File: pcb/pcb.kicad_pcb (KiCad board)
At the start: 2 copper layers, 156.4 x 122.7 mm, 68 parts, among them SW1 SW_Push, SW10 SW_Push, SW11 SW_Push, SW12 SW_Push, SW13 SW_Push, SW14 SW_Push, SW15 SW_Push, SW16 SW_Push, SW17 SW_Push, SW18 SW_Push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

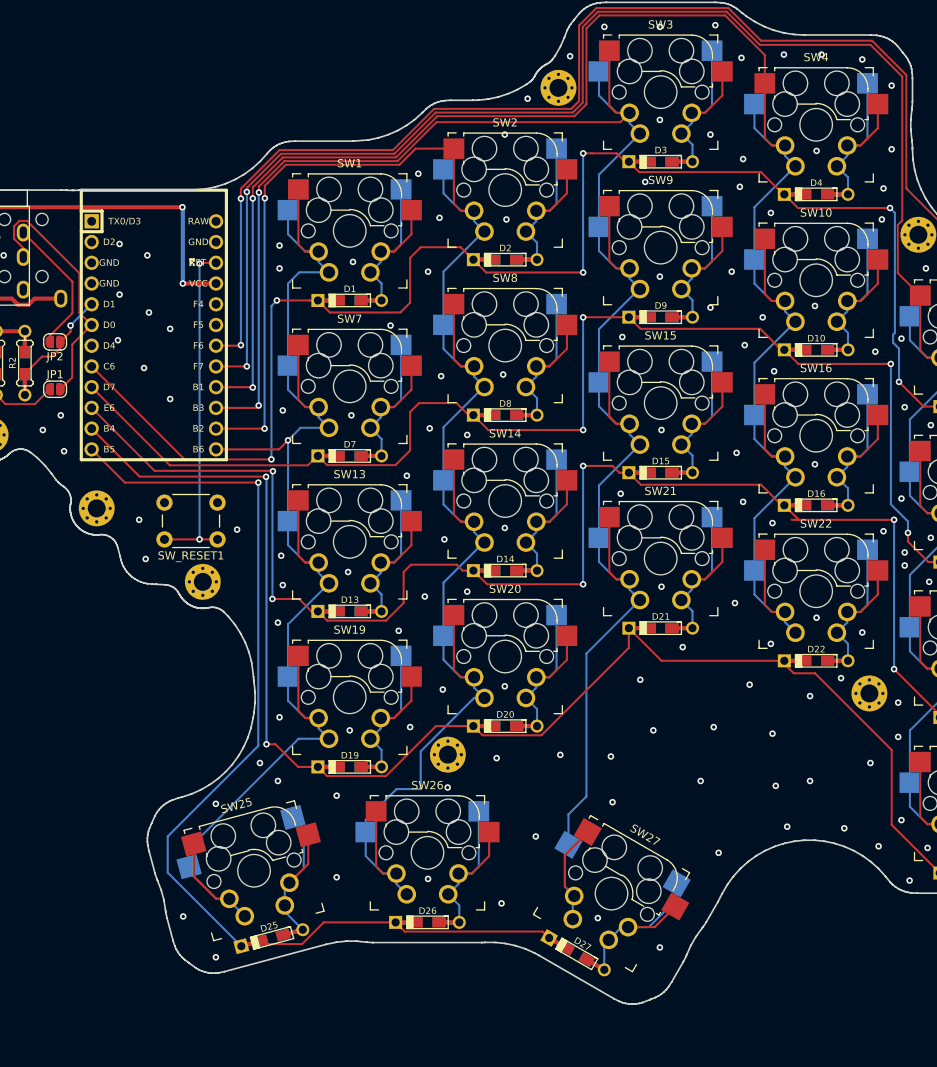
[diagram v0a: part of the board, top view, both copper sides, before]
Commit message: Redesign thumb cluster
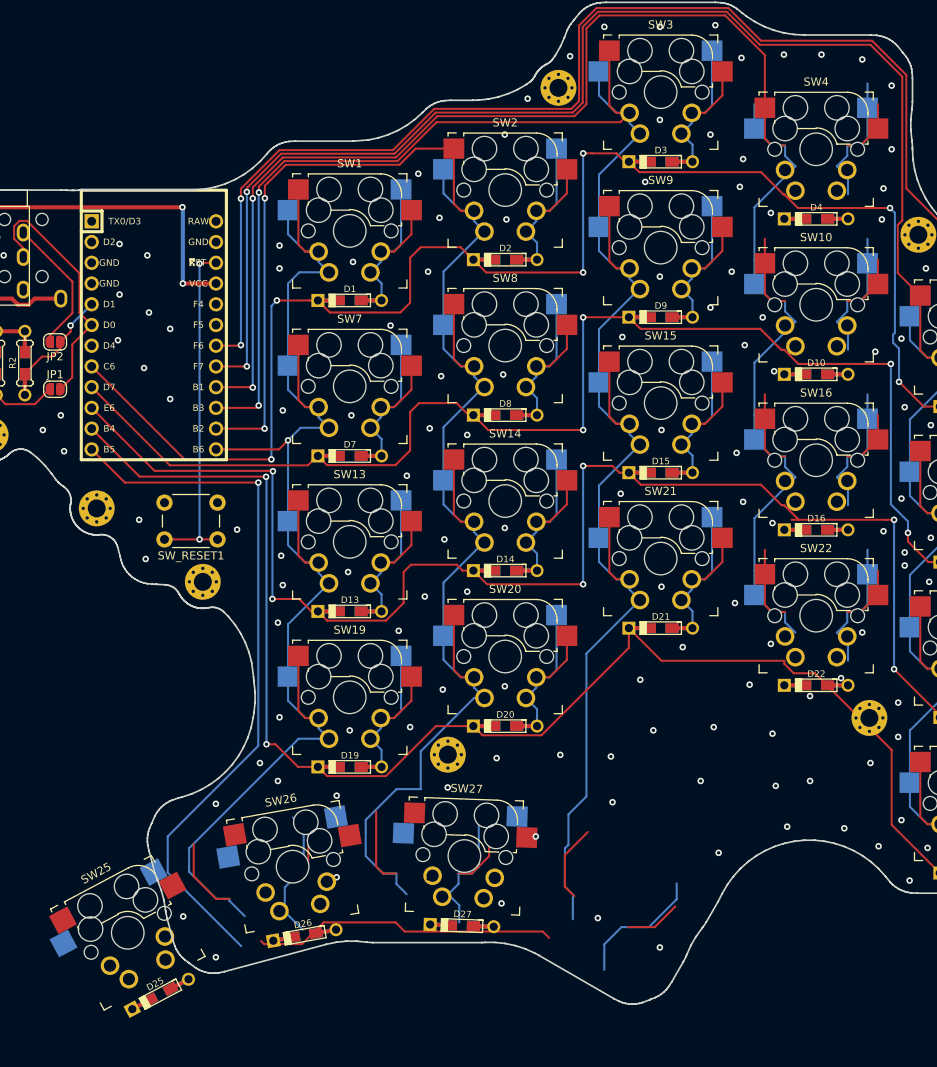
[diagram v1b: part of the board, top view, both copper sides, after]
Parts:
- moved SW27 18.6 mm to (14.1, 81.6), turned to 358 degrees
- moved SW25 17.2 mm to (-27.2, 91.0), turned to 28 degrees
- moved SW26 16.6 mm to (-7.00, 82.9), turned to 10 degrees
- moved D25 15.3 mm to (-23.2, 98.5), turned to 208 degrees
- moved D26 15.1 mm to (-5.52, 91.3), turned to 190 degrees
- moved D27 14.5 mm to (13.8, 90.1), turned to 178 degrees
- moved D4 3.00 mm to (57.1, 3.52)
- moved D10 3.00 mm to (57.1, 22.6)
- moved D16 3.00 mm to (57.1, 41.6)
- moved D22 3.00 mm to (57.1, 60.7)
- moved SW10 3.00 mm to (57.1, 14.1)
- moved SW16 3.00 mm to (57.1, 33.1)
- moved SW22 3.00 mm to (57.1, 52.1)
- moved SW4 3.00 mm to (57.1, -5.00)
- moved generated 3.00 mm to (63.7, 64.7)
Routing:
- net (no net): track 0.00 -> 43.0 mm, vias 0 -> 5
- net /row4: track 124.6 -> 87.2 mm
- net Net-(D25-Pad2): track 23.0 -> 0.00 mm, vias 0 -> 3
- net Net-(D26-Pad2): track 24.2 -> 37.4 mm, vias 0 -> 2
- net /col0: track 179.2 -> 169.7 mm
- net /col2: track 255.8 -> 263.0 mm, vias 2 -> 3
- net /col1: track 227.6 -> 234.2 mm
- net Net-(D27-Pad2): vias 0 -> 2
- net GND: vias 170 -> 157

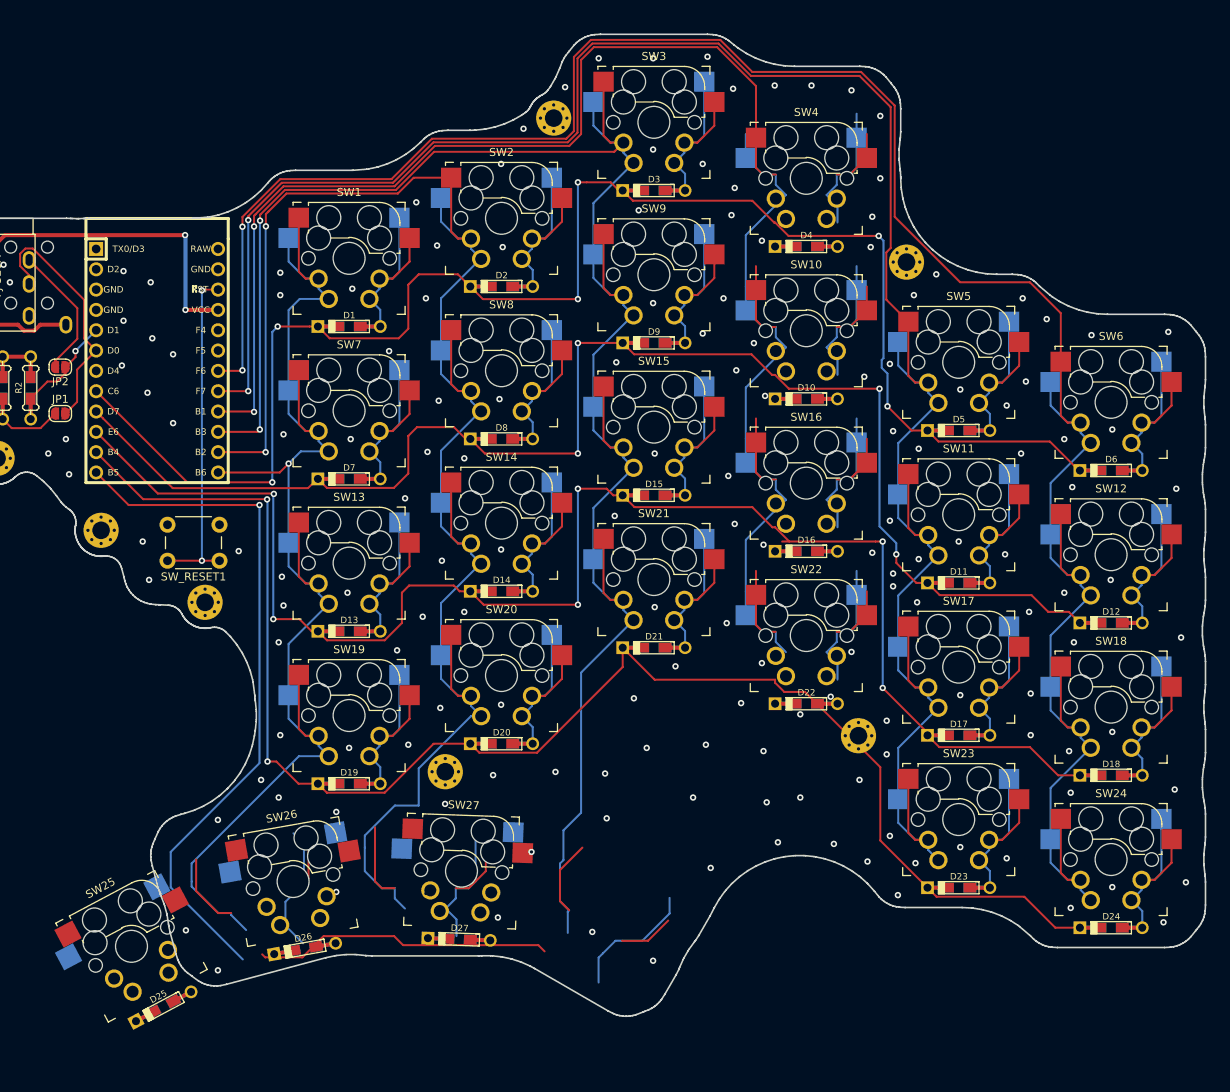
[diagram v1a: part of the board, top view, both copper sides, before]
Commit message: Adjust key placement
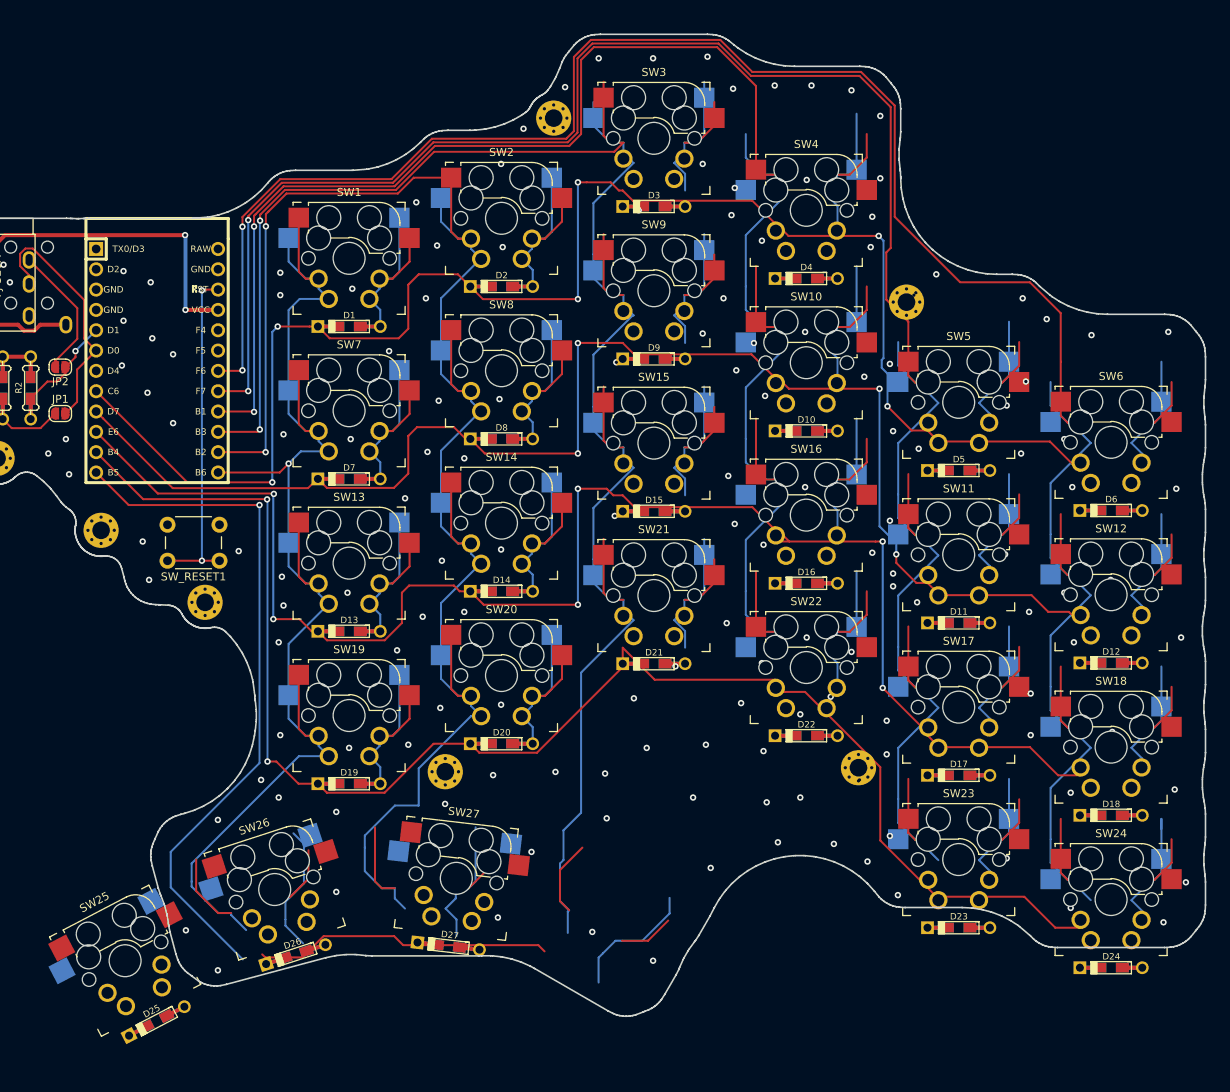
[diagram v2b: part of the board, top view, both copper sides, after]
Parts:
- removed the generated at (63.7, 64.7)
- removed the generated at (69.7, 5.47)
- added generated: MountingHole_2.2mm_M2_Pad_Via, MountingHole_2.2mm_M2_Pad_Via, F.Cu at (63.7, 68.7)
- added generated: MountingHole_2.2mm_M2_Pad_Via, MountingHole_2.2mm_M2_Pad_Via, F.Cu at (69.7, 10.5)
- moved D11 5.00 mm to (76.2, 50.6)
- moved D12 5.00 mm to (95.2, 55.6)
- moved D17 5.00 mm to (76.2, 69.6)
- moved D18 5.00 mm to (95.2, 74.6)
- moved D23 5.00 mm to (76.2, 88.7)
- moved D24 5.00 mm to (95.2, 93.7)
- moved D5 5.00 mm to (76.2, 31.5)
- moved D6 5.00 mm to (95.2, 36.5)
- moved SW11 5.00 mm to (76.2, 42.0)
- moved SW12 5.00 mm to (95.2, 47.0)
- moved SW17 5.00 mm to (76.2, 61.1)
- moved SW23 5.00 mm to (76.2, 80.2)
- moved SW24 5.00 mm to (95.2, 85.2)
- moved SW5 5.00 mm to (76.2, 23.0)
- moved SW6 5.00 mm to (95.2, 28.0)
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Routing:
- net (no net): track 43.0 -> 133.9 mm, vias 5 -> 25
- net /row4: track 87.2 -> 124.6 mm
- net Net-(D26-Pad2): track 37.4 -> 16.2 mm
- net Net-(D27-Pad2): track 23.1 -> 39.7 mm, vias 2 -> 1
- net /col2: track 263.0 -> 246.3 mm
- net /col1: track 234.2 -> 218.0 mm
- net Net-(D12-Pad2): track 24.2 -> 16.7 mm
- net Net-(D11-Pad2): track 24.2 -> 16.7 mm
- net Net-(D6-Pad2): track 24.2 -> 16.7 mm
- net Net-(D5-Pad2): track 24.2 -> 16.7 mm, vias 0 -> 1
- net Net-(D24-Pad2): track 25.5 -> 17.9 mm
- net Net-(D23-Pad2): track 24.2 -> 16.7 mm
- net Net-(D18-Pad2): track 24.2 -> 16.7 mm
- net Net-(D17-Pad2): track 24.2 -> 16.7 mm
- net Net-(D4-Pad2): track 24.2 -> 16.7 mm
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
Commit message: Update pcb
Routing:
- net (no net): track 133.9 -> 0.00 mm, vias 25 -> 1
- net /col0: track 169.7 -> 198.3 mm
- net /col1: track 218.0 -> 244.7 mm, vias 2 -> 3
- net Net-(D25-Pad2): track 0.00 -> 22.9 mm, vias 3 -> 0
- net Net-(D27-Pad2): track 39.7 -> 24.0 mm, vias 1 -> 0
- net /col2: track 246.3 -> 260.7 mm
- net Net-(D18-Pad2): track 16.7 -> 24.2 mm
- net Net-(D12-Pad2): track 16.7 -> 24.2 mm
- net Net-(D11-Pad2): track 16.7 -> 24.2 mm
- net Net-(D6-Pad2): track 16.7 -> 24.2 mm
- net Net-(D23-Pad2): track 16.7 -> 24.2 mm
- net Net-(D5-Pad2): track 16.7 -> 24.2 mm, vias 1 -> 0
- net Net-(D22-Pad2): track 16.7 -> 24.2 mm
- net Net-(D17-Pad2): track 16.7 -> 24.2 mm
- net Net-(D16-Pad2): track 16.7 -> 24.2 mm
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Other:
- board size 156.4 x 122.7 mm -> 156.4 x 127.2 mm

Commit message: Small tweaks, regenerate PCB
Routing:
- net GND: vias 101 -> 110

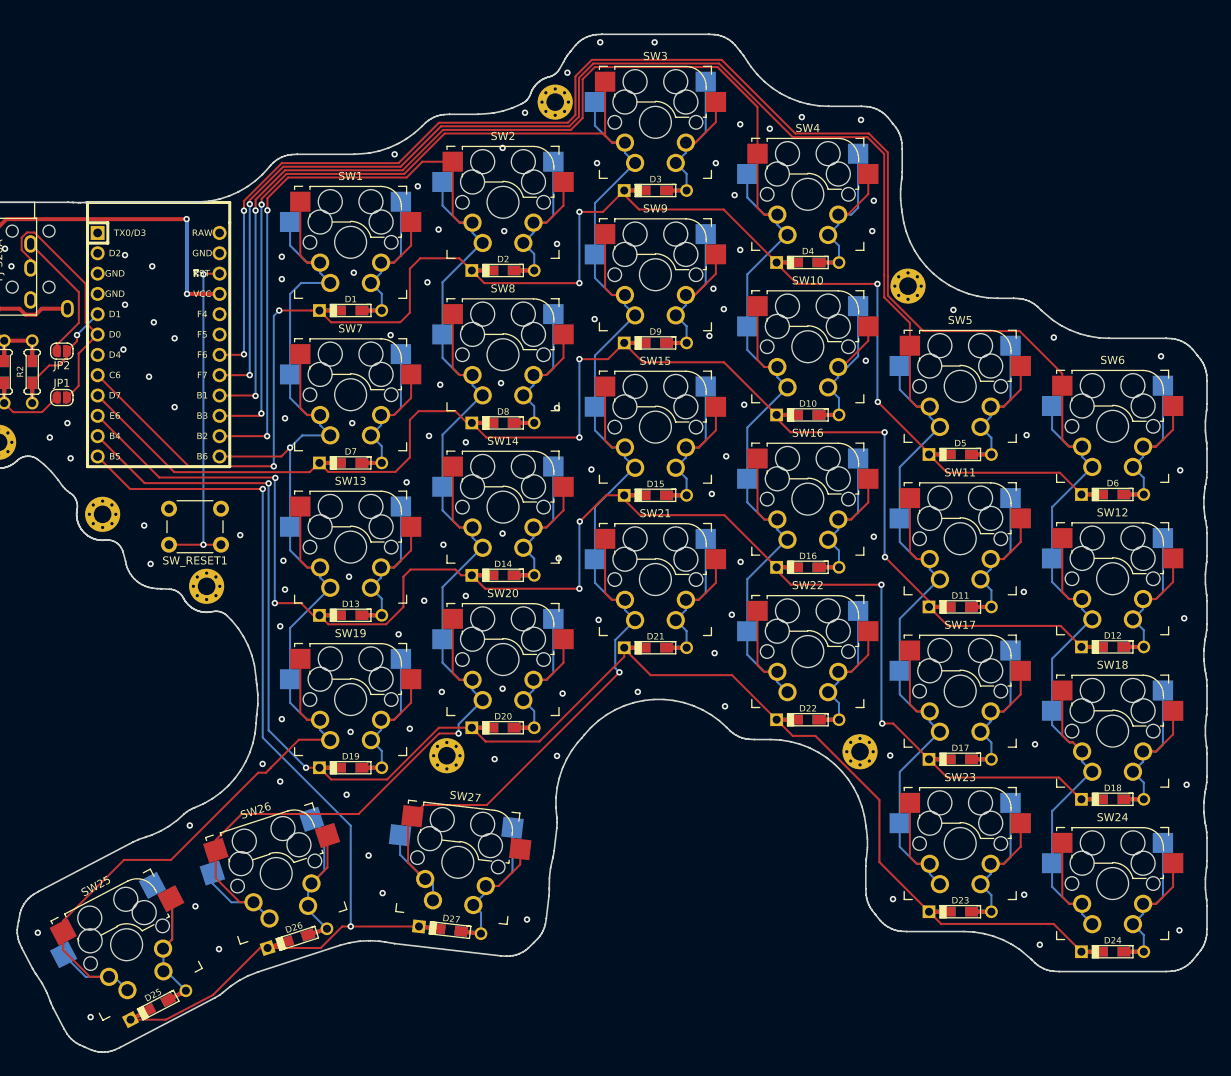
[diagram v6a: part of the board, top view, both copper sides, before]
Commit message: Change the column offsets post 1 fab
After 1 fab keyboard seemed to be too aggressive. Boo hoo.
Lessons learned. New measurments. And halfing it either way.
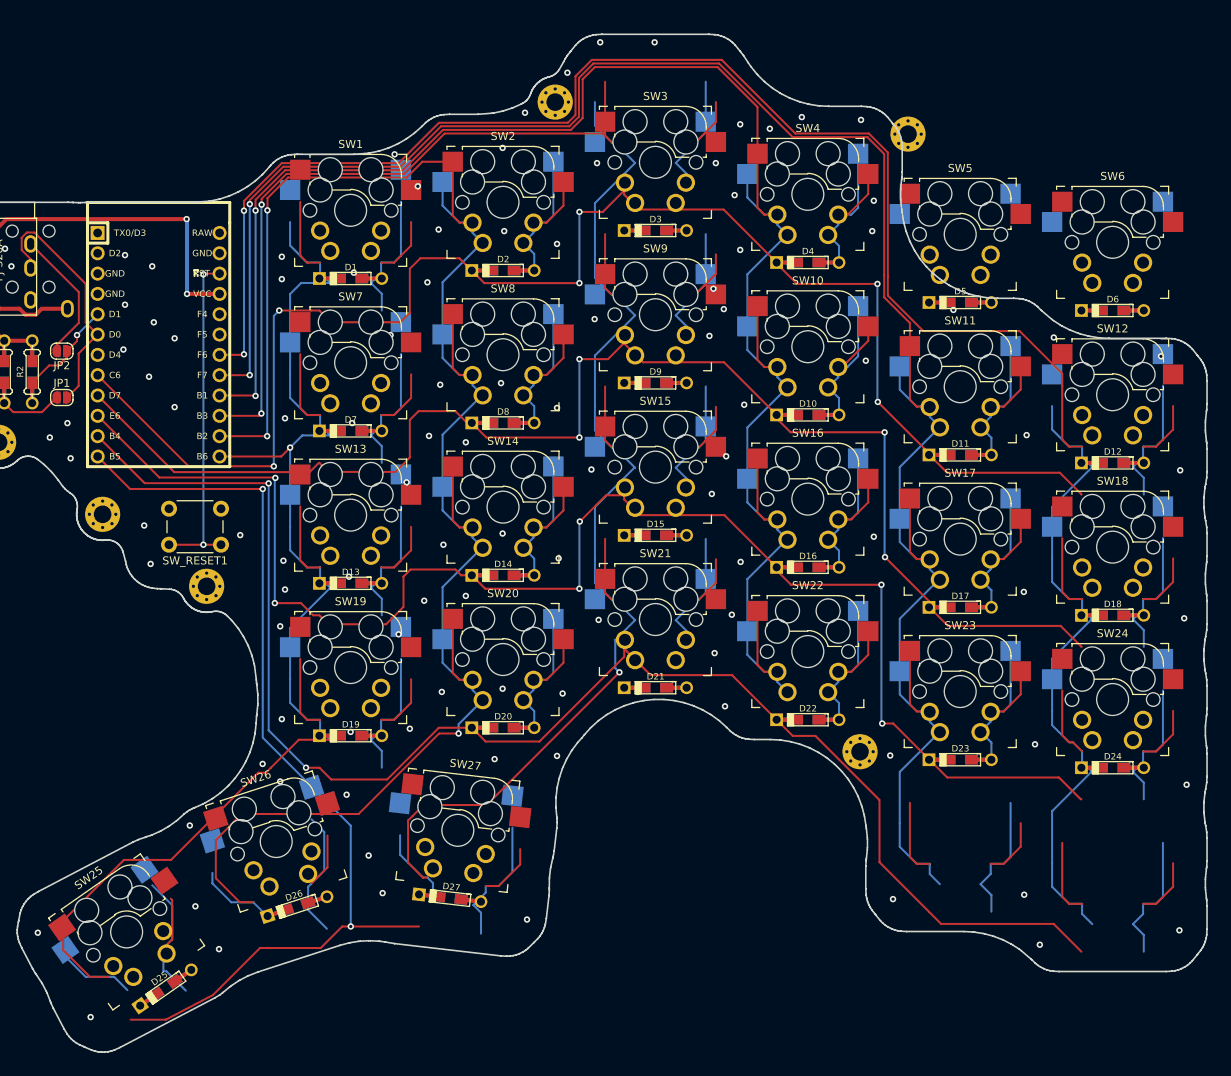
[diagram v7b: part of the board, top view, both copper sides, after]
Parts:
- removed the generated at (12.0, 69.2)
- removed the generated at (69.7, 10.5)
- added generated: MountingHole_2.2mm_M2_Pad_Via, MountingHole_2.2mm_M2_Pad_Via, F.Cu at (69.7, -8.53)
- moved SW24 23.0 mm to (95.2, 62.1)
- moved D18 23.0 mm to (95.2, 51.6)
- moved D24 23.0 mm to (95.2, 70.7)
- moved D6 23.0 mm to (95.2, 13.5)
- moved SW6 23.0 mm to (95.2, 5.00)
- moved SW12 23.0 mm to (95.2, 24.1)
- moved D12 23.0 mm to (95.2, 32.6)
- moved SW18 23.0 mm to (95.2, 43.1)
- moved SW23 19.0 mm to (76.2, 61.1)
- moved D17 19.0 mm to (76.2, 50.6)
- moved D23 19.0 mm to (76.2, 69.7)
- moved D5 19.0 mm to (76.2, 12.5)
- moved SW17 19.0 mm to (76.2, 42.1)
- moved SW5 19.0 mm to (76.2, 4.00)
- moved SW11 19.0 mm to (76.2, 23.1)
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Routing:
- net (no net): track 0.00 -> 163.3 mm
- net /col2: track 260.7 -> 117.0 mm, vias 3 -> 2
- net Net-(D5-Pad2): track 24.2 -> 0.00 mm
- net Net-(D23-Pad2): track 24.2 -> 48.5 mm
- net /row4: track 121.9 -> 142.4 mm
- net Net-(D24-Pad2): track 24.2 -> 40.9 mm
- net Net-(D6-Pad2): track 24.2 -> 7.58 mm
- net /col1: track 244.7 -> 234.5 mm
- net Net-(D21-Pad2): track 24.2 -> 16.7 mm
- net Net-(D15-Pad2): track 24.2 -> 16.7 mm
- net Net-(D3-Pad2): track 23.7 -> 16.4 mm
- net Net-(D9-Pad2): track 23.6 -> 16.4 mm, vias 0 -> 1
